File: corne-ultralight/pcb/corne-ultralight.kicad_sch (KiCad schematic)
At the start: 96 parts, among them J2 OLED, J7 OLED, SW1 SW_PUSH, SW10 SW_PUSH, SW11 SW_PUSH, SW12 SW_PUSH, SW13 SW_PUSH, SW14 SW_PUSH, SW15 SW_PUSH, SW16 SW_PUSH, SW17 SW_PUSH, SW18 SW_PUSH, SW19 SW_PUSH, SW2 SW_PUSH, SW20 SW_PUSH, SW21 SW_PUSH, SW22 SW_PUSH, SW23 SW_PUSH, SW24 SW_PUSH, SW25 SW_PUSH, SW26 SW_PUSH, SW27 SW_PUSH, SW28 SW_PUSH, SW29 SW_PUSH, SW3 SW_PUSH, SW30 SW_PUSH, SW31 SW_PUSH, SW32 SW_PUSH, SW33 SW_PUSH, SW34 SW_PUSH, SW35 SW_PUSH, SW36 SW_PUSH, SW37 SW_PUSH, SW38 SW_PUSH, SW39 SW_PUSH, SW4 SW_PUSH, SW40 SW_PUSH, SW41 SW_PUSH, SW42 SW_PUSH, SW5 SW_PUSH, SW6 SW_PUSH, SW7 SW_PUSH, SW8 SW_PUSH, SW9 SW_PUSH, U1 ProMicro, U2 ProMicro

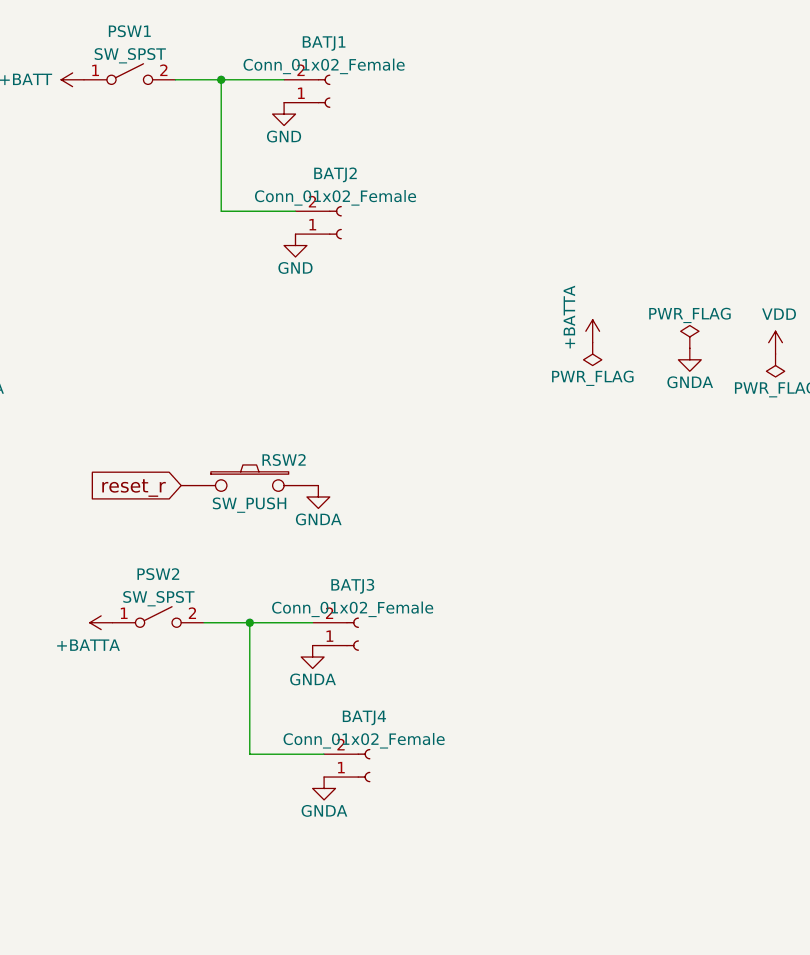
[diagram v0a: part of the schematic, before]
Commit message: Adjust JST polarity.
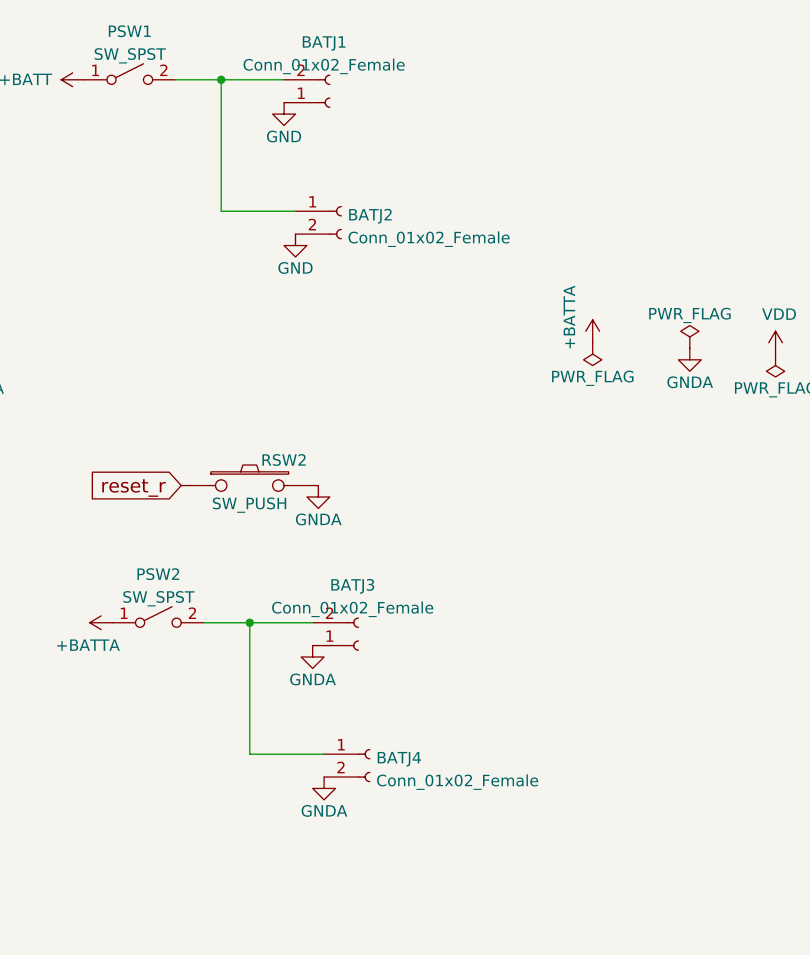
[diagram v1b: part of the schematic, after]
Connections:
- net GND: now also BATJ2.2 (Pin_2); no longer BATJ2.1 (Pin_1)
- net GNDA: now also BATJ4.2 (Pin_2); no longer BATJ4.1 (Pin_1)
- net at BATJ3.2 (Pin_2), PSW2.2 (B): now also BATJ4.1 (Pin_1); no longer BATJ4.2 (Pin_2)
- net at BATJ1.2 (Pin_2), PSW1.2 (B): now also BATJ2.1 (Pin_1); no longer BATJ2.2 (Pin_2)
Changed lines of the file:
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@@
     (pin "1")
   )
-  (symbol (lib_id "Connector:Conn_01x02_Female") (at 233.045 135.89 0) (mirror x) (unit 1)
+  (symbol (lib_id "Connector:Conn_01x02_Female") (at 233.045 133.35 0) (unit 1)
     (in_bom yes) (on_board yes) (fields_autoplaced)
-    (property "Reference" "BATJ4" (id 0) (at 232.41 129.193 0))
-    (property "Value" "Conn_01x02_Female" (id 1) (at 232.41 131.7299 0))
-    (property "Footprint" "Connector_JST:JST_PH_S2B-PH-K_1x02_P2.00mm_Horizontal" (id 2) (at 233.045 135.89 0)
+    (property "Reference" "BATJ4" (id 0) (at 233.7562 133.7853 0)
+      (effects (font (size 1.27 1.27)) (justify left))
+    )
+    (property "Value" "Conn_01x02_Female" (id 1) (at 233.7562 136.3222 0)
+      (effects (font (size 1.27 1.27)) (justify left))
+    )
+    (property "Footprint" "Connector_JST:JST_PH_S2B-PH-K_1x02_P2.00mm_Horizontal" (id 2) (at 233.045 133.35 0)
       (effects (font (size 1.27 1.27)) hide)
     )
-    (property "Datasheet" "~" (id 3) (at 233.045 135.89 0)
+    (property "Datasheet" "~" (id 3) (at 233.045 133.35 0)
       (effects (font (size 1.27 1.27)) hide)
     )
@@
     (pin "1")
   )
-  (symbol (lib_id "Connector:Conn_01x02_Female") (at 229.87 75.565 0) (mirror x) (unit 1)
+  (symbol (lib_id "Connector:Conn_01x02_Female") (at 229.87 73.025 0) (unit 1)
     (in_bom yes) (on_board yes) (fields_autoplaced)
-    (property "Reference" "BATJ2" (id 0) (at 229.235 68.868 0))
-    (property "Value" "Conn_01x02_Female" (id 1) (at 229.235 71.4049 0))
-    (property "Footprint" "Connector_JST:JST_PH_S2B-PH-K_1x02_P2.00mm_Horizontal" (id 2) (at 229.87 75.565 0)
+    (property "Reference" "BATJ2" (id 0) (at 230.5812 73.4603 0)
+      (effects (font (size 1.27 1.27)) (justify left))
+    )
+    (property "Value" "Conn_01x02_Female" (id 1) (at 230.5812 75.9972 0)
+      (effects (font (size 1.27 1.27)) (justify left))
+    )
+    (property "Footprint" "Connector_JST:JST_PH_S2B-PH-K_1x02_P2.00mm_Horizontal" (id 2) (at 229.87 73.025 0)
       (effects (font (size 1.27 1.27)) hide)
     )
-    (property "Datasheet" "~" (id 3) (at 229.87 75.565 0)
+    (property "Datasheet" "~" (id 3) (at 229.87 73.025 0)
       (effects (font (size 1.27 1.27)) hide)
     )

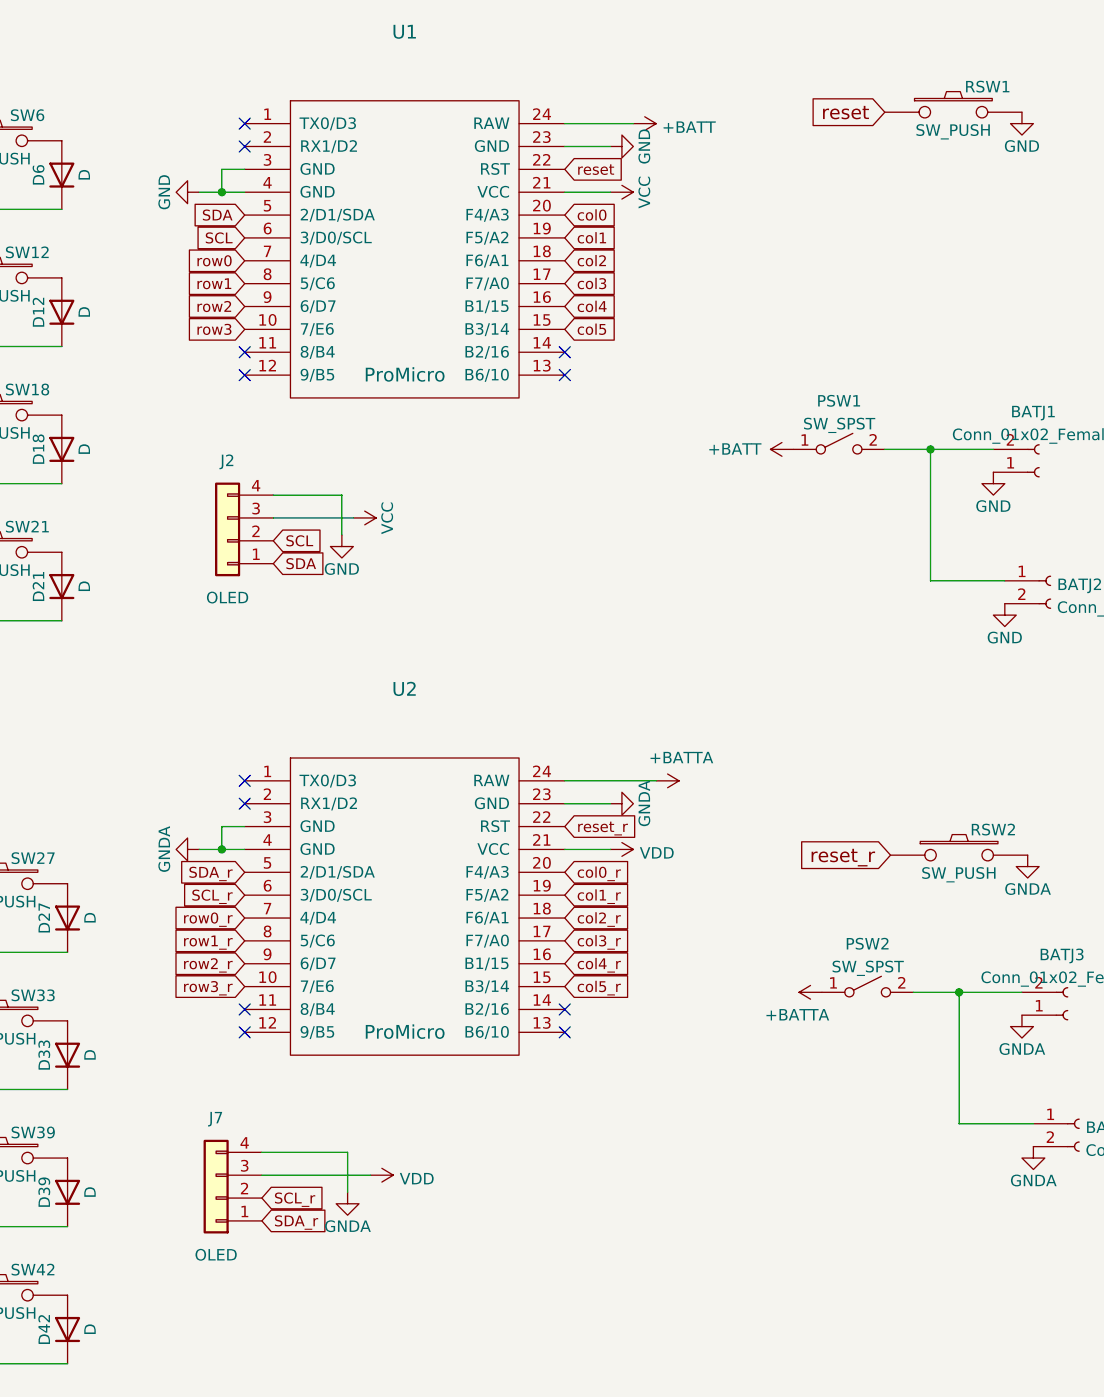
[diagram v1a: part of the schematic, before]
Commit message: Add test points for RGB strip.
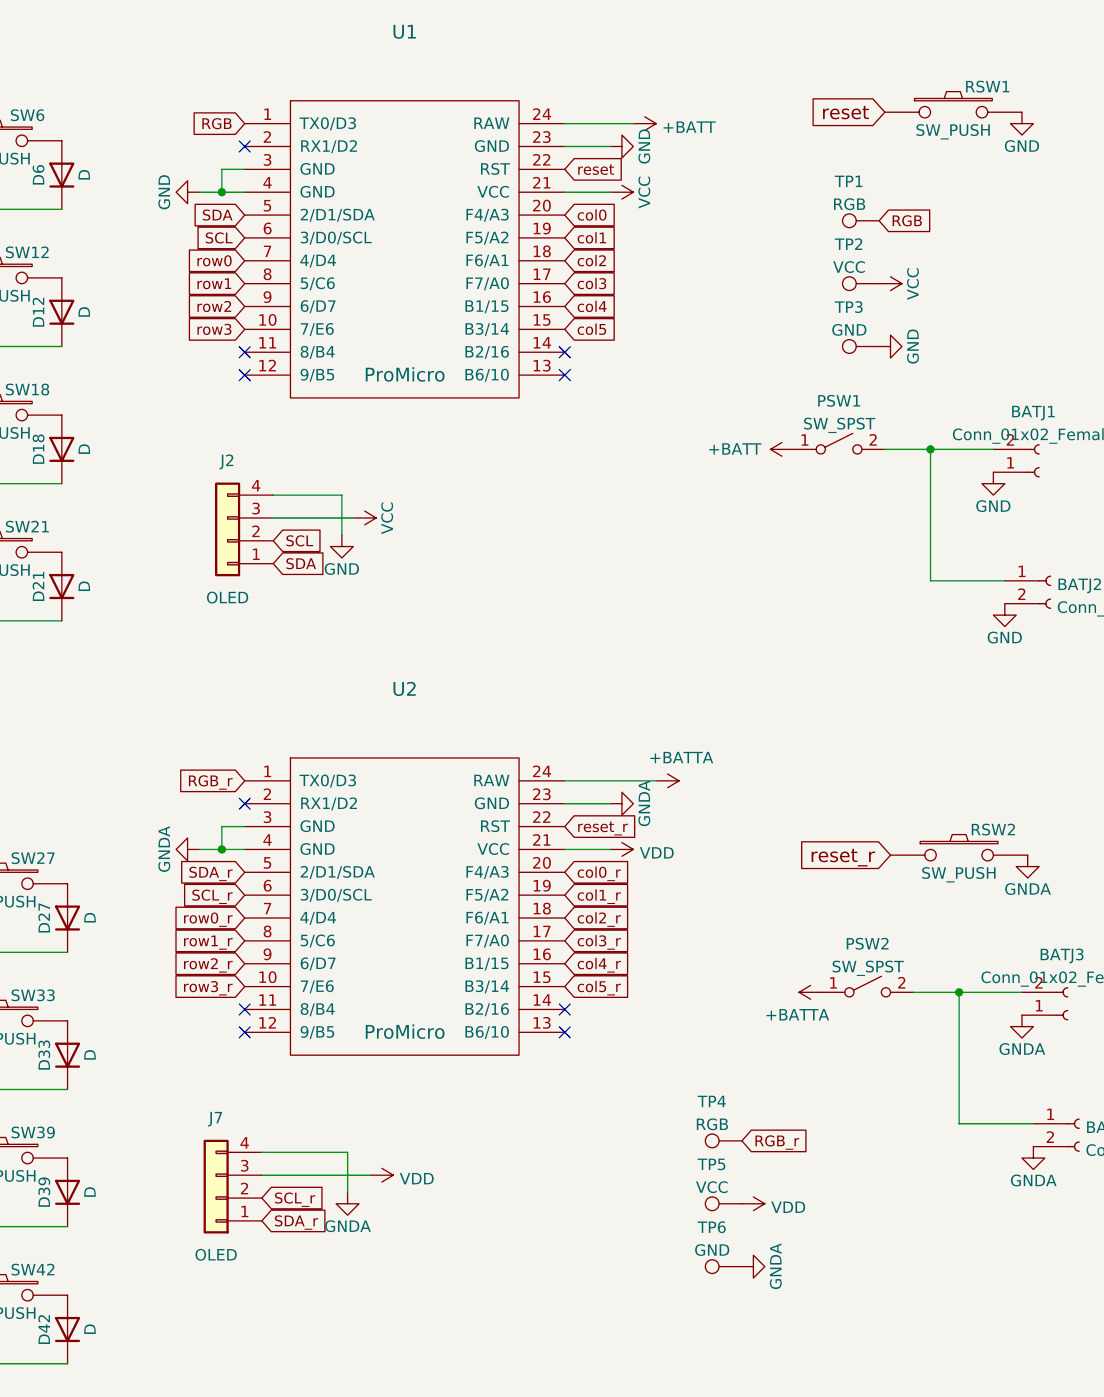
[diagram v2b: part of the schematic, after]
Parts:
- added TP1, TP4: RGB, TestPoint:TestPoint_Pad_D1.5mm, symbol Connector:TestPoint
- added TP2, TP5: VCC, TestPoint:TestPoint_Pad_D1.5mm, symbol Connector:TestPoint
- added TP3, TP6: GND, TestPoint:TestPoint_Pad_D1.5mm, symbol Connector:TestPoint
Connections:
- net GND: now also TP3.1
- net GNDA: now also TP6.1
- net VCC: now also TP2.1
- net VDD: now also TP5.1
- net RGB: now reaches U1.1 (TX0/D3)
- net RGB: now also TP1.1
- net RGB_r: now reaches U2.1 (TX0/D3)
- net RGB_r: now also TP4.1
- no-connect marks 12 -> 10

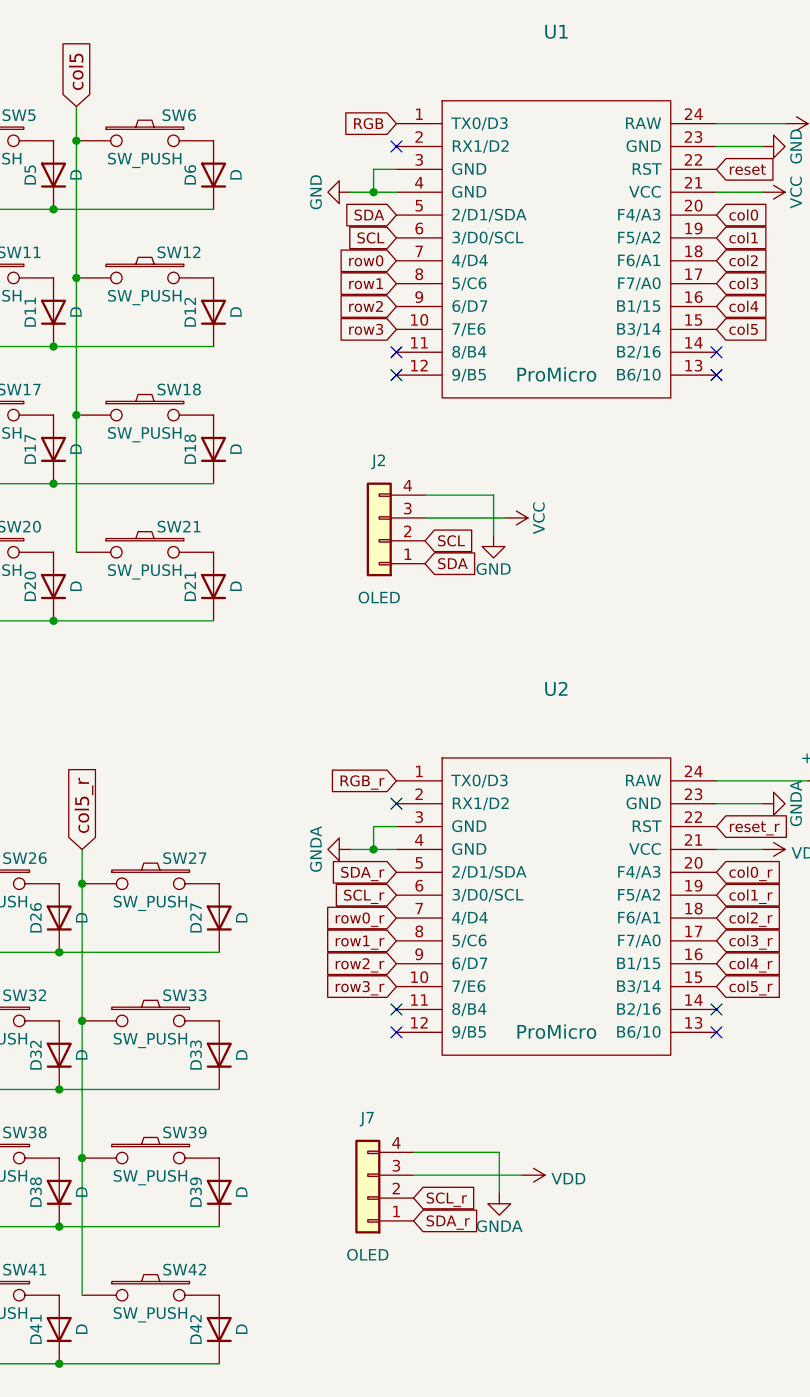
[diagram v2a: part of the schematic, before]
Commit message: Switch to nice!view display header.
* Route extra pin and move header to be centered for
  nice!view display support.
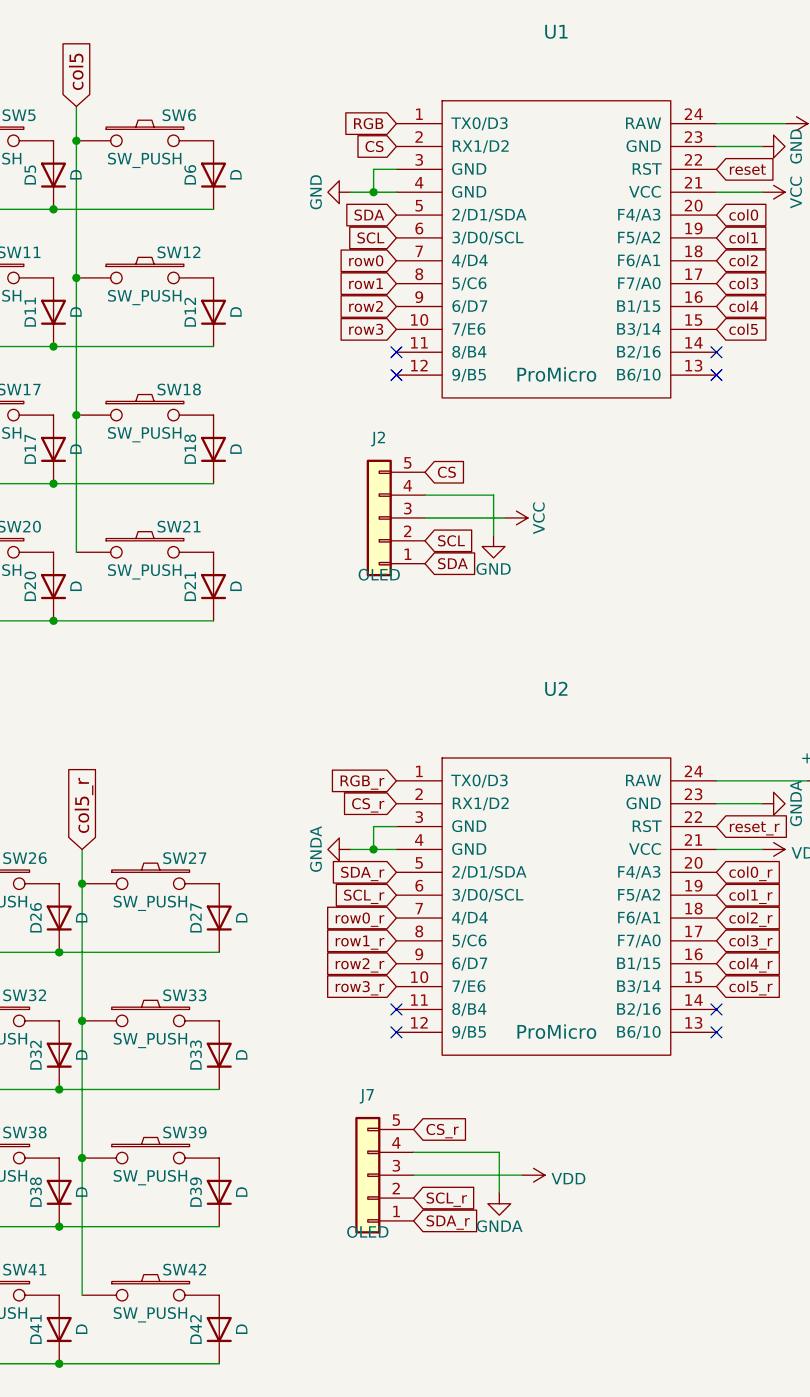
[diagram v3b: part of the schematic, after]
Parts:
- J2, J7: footprint kbd:OLED_1side -> nice_view:nice_view_1side; symbol Connector_Generic:Conn_01x04 -> Connector_Generic:Conn_01x05
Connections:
- net CS: now reaches U1.2 (RX1/D2)
- net CS: now also J2.5 (Pin_5)
- net CS_r: now reaches U2.2 (RX1/D2)
- net CS_r: now also J7.5 (Pin_5)
- no-connect marks 10 -> 8
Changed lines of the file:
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@@
   (junction (at 48.895 46.99) (diameter 0) (color 0 0 0 0)
   )
-  (no_connect (at 140.335 24.765))
   (no_connect (at 175.895 47.625))
   (no_connect (at 140.335 123.19))
@@
   (no_connect (at 175.895 50.165))
   (no_connect (at 140.335 120.65))
-  (no_connect (at 140.335 97.79))
   (no_connect (at 175.895 120.65))
   (wire (pts (xy 104.775 54.61) (xy 104.775 69.85))
@@
     )
   )
+  (global_label "CS" (shape input) (at 143.51 60.96 0) (fields_autoplaced)
+    (effects (font (size 1.1938 1.1938)) (justify left))
+    (property "Intersheet References" "${INTERSHEET_REFS}" (id 0) (at 148.0254 60.8854 0)
+      (effects (font (size 1.1938 1.1938)) (justify left) hide)
+    )
+  )
   (global_label "col3" (shape input) (at 69.215 20.32 90) (fields_autoplaced)
     (effects (font (size 1.524 1.524)) (justify left))
@@
     )
   )
+  (global_label "CS" (shape input) (at 140.335 24.765 180) (fields_autoplaced)
+    (effects (font (size 1.1938 1.1938)) (justify right))
+    (property "Intersheet References" "${INTERSHEET_REFS}" (id 0) (at 135.8196 24.8396 0)
+      (effects (font (size 1.1938 1.1938)) (justify right) hide)
+    )
+  )
   (global_label "SDA" (shape input) (at 143.51 71.12 0) (fields_autoplaced)
     (effects (font (size 1.1938 1.1938)) (justify left))
@@
     )
   )
+  (global_label "CS_r" (shape input) (at 142.24 133.985 0) (fields_autoplaced)
+    (effects (font (size 1.1938 1.1938)) (justify left))
+    (property "Intersheet References" "${INTERSHEET_REFS}" (id 0) (at 148.4039 134.0596 0)
+      (effects (font (size 1.1938 1.1938)) (justify left) hide)
+    )
+  )
   (global_label "col3_r" (shape input) (at 175.895 113.03 0) (fields_autoplaced)
     (effects (font (size 1.1938 1.1938)) (justify left))
@@
     (property "Intersheet References" "${INTERSHEET_REFS}" (id 0) (at 0 0 0)
       (effects (font (size 1.27 1.27)) hide)
+    )
+  )
+  (global_label "CS_r" (shape input) (at 140.335 97.79 180) (fields_autoplaced)
+    (effects (font (size 1.1938 1.1938)) (justify right))
+    (property "Intersheet References" "${INTERSHEET_REFS}" (id 0) (at 134.1711 97.7154 0)
+      (effects (font (size 1.1938 1.1938)) (justify right) hide)
     )
   )
@@
     (pin "1")
   )
-  (symbol (lib_id "Connector_Generic:Conn_01x04") (at 138.43 68.58 180) (unit 1)
-    (in_bom yes) (on_board yes)
-    (property "Reference" "J2" (id 0) (at 138.43 59.69 0))
-    (property "Value" "OLED" (id 1) (at 138.43 74.93 0))
-    (property "Footprint" "kbd:OLED_1side" (id 2) (at 138.43 68.58 0)
-      (effects (font (size 1.27 1.27)) hide)
-    )
-    (property "Datasheet" "" (id 3) (at 138.43 68.58 0)
+  (symbol (lib_id "Connector_Generic:Conn_01x05") (at 138.43 66.04 180) (unit 1)
+    (in_bom yes) (on_board yes)
+    (property "Reference" "J2" (id 0) (at 138.43 57.15 0))
+    (property "Value" "OLED" (id 1) (at 138.43 72.39 0))
+    (property "Footprint" "nice_view:nice_view_1side" (id 2) (at 138.43 66.04 0)
+      (effects (font (size 1.27 1.27)) hide)
+    )
+    (property "Datasheet" "~" (id 3) (at 138.43 66.04 0)
       (effects (font (size 1.27 1.27)) hide)
     )
@@
     (pin "3")
     (pin "4")
+    (pin "5")
   )
   (symbol (lib_id "power:GND") (at 151.13 67.945 0) (unit 1)
@@
     (pin "1")
   )
-  (symbol (lib_id "Connector_Generic:Conn_01x04") (at 137.16 141.605 180) (unit 1)
-    (in_bom yes) (on_board yes)
-    (property "Reference" "J7" (id 0) (at 137.16 132.715 0))
-    (property "Value" "OLED" (id 1) (at 137.16 147.955 0))
-    (property "Footprint" "kbd:OLED_1side" (id 2) (at 137.16 141.605 0)
-      (effects (font (size 1.27 1.27)) hide)
-    )
-    (property "Datasheet" "" (id 3) (at 137.16 141.605 0)
+  (symbol (lib_id "Connector_Generic:Conn_01x05") (at 137.16 139.065 180) (unit 1)
+    (in_bom yes) (on_board yes)
+    (property "Reference" "J7" (id 0) (at 137.16 130.175 0))
+    (property "Value" "OLED" (id 1) (at 137.16 145.415 0))
+    (property "Footprint" "nice_view:nice_view_1side" (id 2) (at 137.16 139.065 0)
+      (effects (font (size 1.27 1.27)) hide)
+    )
+    (property "Datasheet" "~" (id 3) (at 137.16 139.065 0)
       (effects (font (size 1.27 1.27)) hide)
     )
@@
     (pin "3")
     (pin "4")
+    (pin "5")
   )
   (symbol (lib_id "power:GNDA") (at 151.765 140.97 0) (unit 1)
@@
     )
     (path "/00000000-0000-0000-0000-00005a91da4b"
-      (reference "J2") (unit 1) (value "OLED") (footprint "kbd:OLED_1side")
+      (reference "J2") (unit 1) (value "OLED") (footprint "nice_view:nice_view_1side")
     )
     (path "/00000000-0000-0000-0000-00005c25f9a2"
-      (reference "J7") (unit 1) (value "OLED") (footprint "kbd:OLED_1side")
+      (reference "J7") (unit 1) (value "OLED") (footprint "nice_view:nice_view_1side")
     )
     (path "/2c5bd6d0-044f-48cc-8551-672fbb4708bc"
